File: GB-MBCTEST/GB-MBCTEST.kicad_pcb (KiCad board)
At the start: 2 copper layers, 51.4 x 61 mm, 36 parts, among them J1 DNF, J2 Conn_02x10_Odd_Even, U1 IS62WV1288DBLL-45H, U10 74LVCH245APW, U11 74LVCH245APW, U12 74LVC1G17, U2 74LVC1G08, U3 MX29LV640ExT, U4 74LVC1G02, U5 AP2114H-3.3, U6 74LVC245APW, U7 74LVC245APW, U8 74LVC8T245PW, U9 74LVC1G07

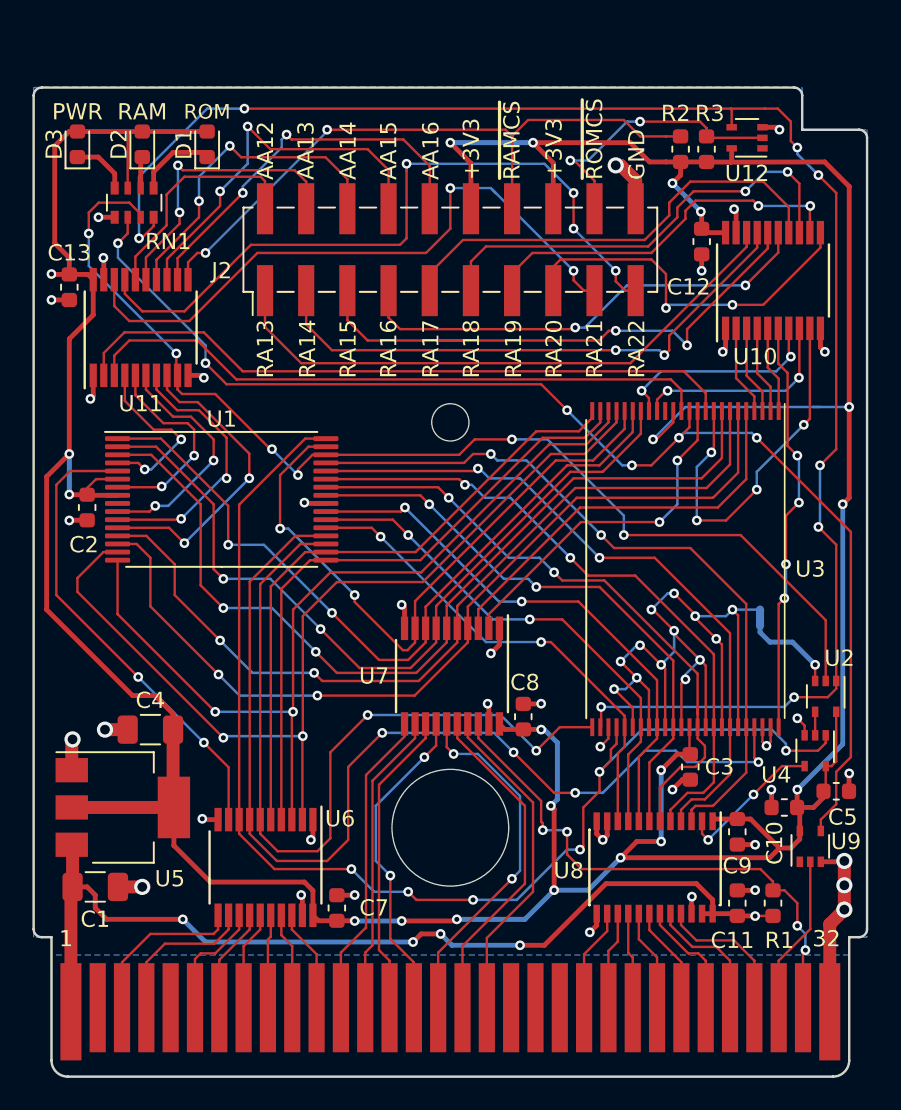
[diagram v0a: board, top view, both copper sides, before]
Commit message: Upgrade most projects to KiCad 6
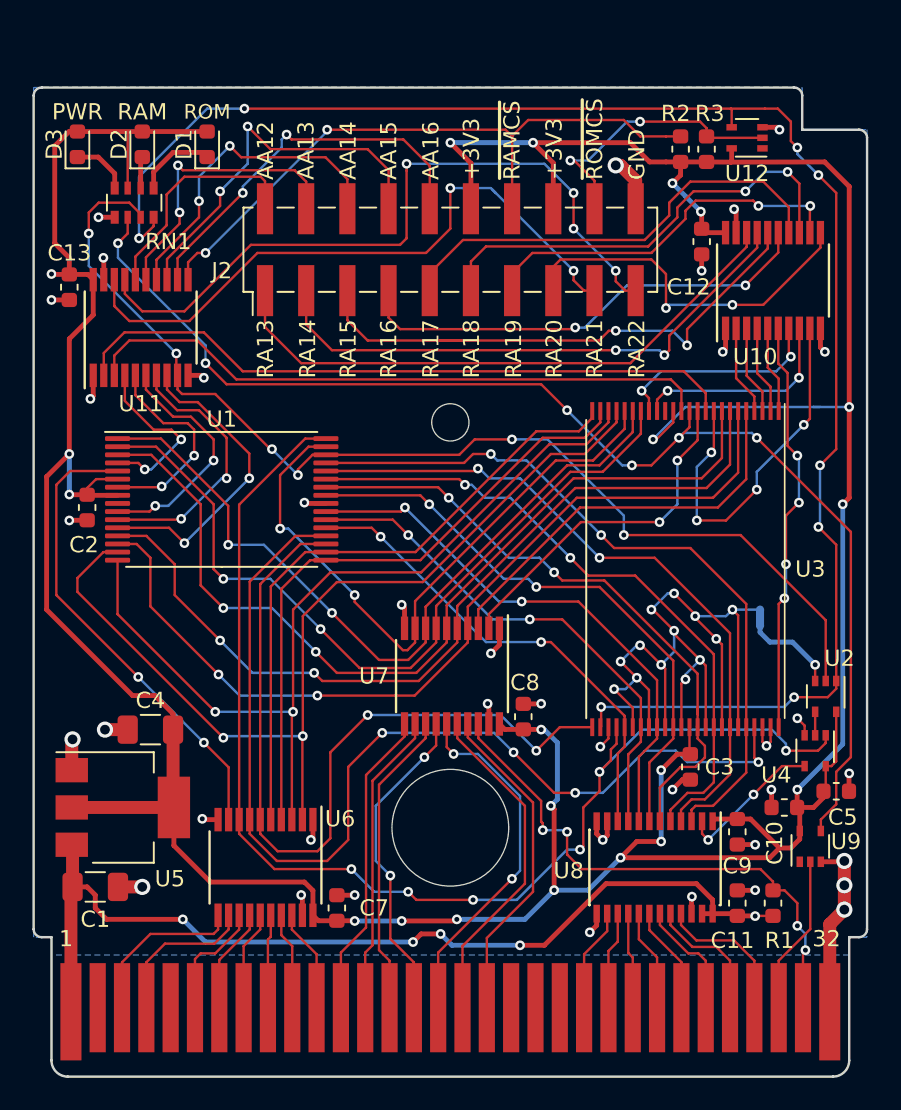
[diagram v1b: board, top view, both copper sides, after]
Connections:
- net /Game Boy Cartridge/~GB_RD renamed /Game Boy Cartridge/~{GB_RD}
- net /Game Boy Cartridge/~GB_WR renamed /Game Boy Cartridge/~{GB_WR}
- net /MBC/~MBC_RAM_CS renamed /MBC/~{MBC_RAM_CS}
- net /MBC/~MBC_ROM_CS renamed /MBC/~{MBC_ROM_CS}
- net /~RAM_CS renamed /~{RAM_CS}
- net /~RAM_WR renamed /~{RAM_WR}
- net /~RD renamed /~{RD}
- net /~RESET renamed /~{RESET}
- net /~ROM_CS renamed /~{ROM_CS}
- net /~ROM_WR renamed /~{ROM_WR}
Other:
- net class Default removed
- board text added: "~{RAMCS}"
- board text added: "~{ROMCS}"
- board text removed: "~RAMCS"
- board text removed: "~ROMCS"
